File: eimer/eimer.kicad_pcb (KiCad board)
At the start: 2 copper layers, 21 x 51 mm, 33 parts, among them J1 Conn_01x20, J2 Conn_01x20, J3 Conn_01x03, J4 USB_C_Receptacle_USB2.0_14P, SW1 SW_Push, U1 RP2040, U2 MCP1700x-330xxTT, U4 W25Q16JVUXIQ TR, Y1 12 MHz

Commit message: more routing
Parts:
- moved R1 21.9 mm to (163.9, 72.9), turned to -90 degrees
- moved R2 19.8 mm to (160.8, 72.9), turned to 90 degrees
- moved C4 4.76 mm to (163.2, 83.8)
- moved C3 4.68 mm to (164.2, 83.1)
- moved C11 4.67 mm to (162.2, 83.5)
- moved C2 3.24 mm to (166.2, 87.3)
- moved C12 3.05 mm to (165.2, 86.9)
- moved R5 1.84 mm to (162.8, 97.0), turned to 180 degrees
- moved U2 1.61 mm to (159.5, 75.8)
- moved R7 1.59 mm to (158.0, 82.0)
- moved C17 1.32 mm to (160.3, 82.0), turned to 180 degrees
- moved C8 1.21 mm to (157.7, 88.5)
- moved C15 1.11 mm to (159.1, 99.4)
- moved C13 1.08 mm to (158.7, 72.7), turned to 180 degrees
- moved Y1 0.74 mm to (161.7, 99.4)
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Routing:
- net +3.3V: track 0.00 -> 22.8 mm, vias 0 -> 2
- net XIN: track 0.00 -> 6.99 mm
- net +1V1: track 0.00 -> 6.34 mm
- net Net-(C16-Pad1): track 0.00 -> 3.40 mm
- net GND: track 0.00 -> 3.36 mm
- net Net-(J4-CC1): track 0.00 -> 1.90 mm
- net Net-(J4-CC2): track 0.00 -> 1.83 mm
- net XOUT: track 0.00 -> 1.60 mm
- net Net-(U1-USB_DP): track 1.40 -> 0.00 mm
- net Net-(U1-USB_DM): track 1.40 -> 0.00 mm
- net QSPI_SS: track 7.60 -> 8.88 mm
- net USB_D+: track 18.6 -> 19.5 mm
- net USB_D-: track 18.9 -> 19.4 mm

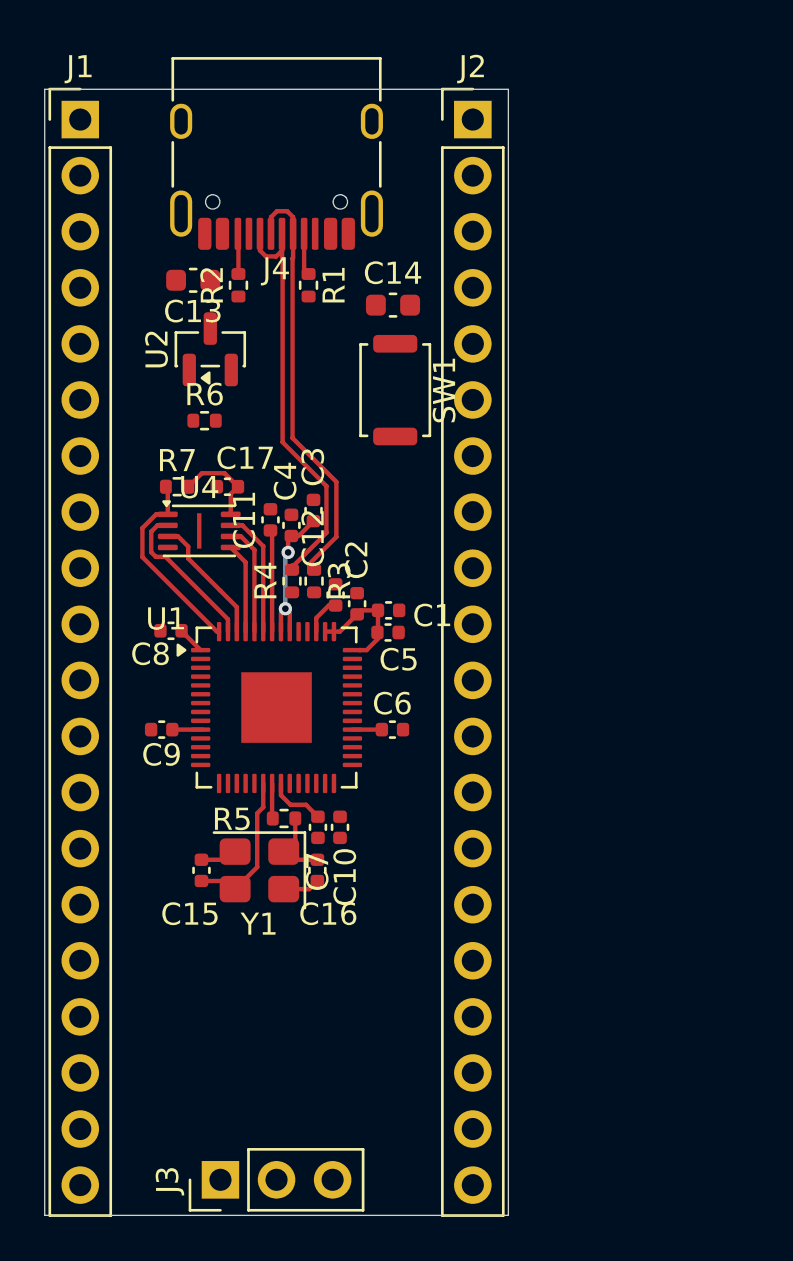
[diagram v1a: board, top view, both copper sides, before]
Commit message: routed left hand side gpios
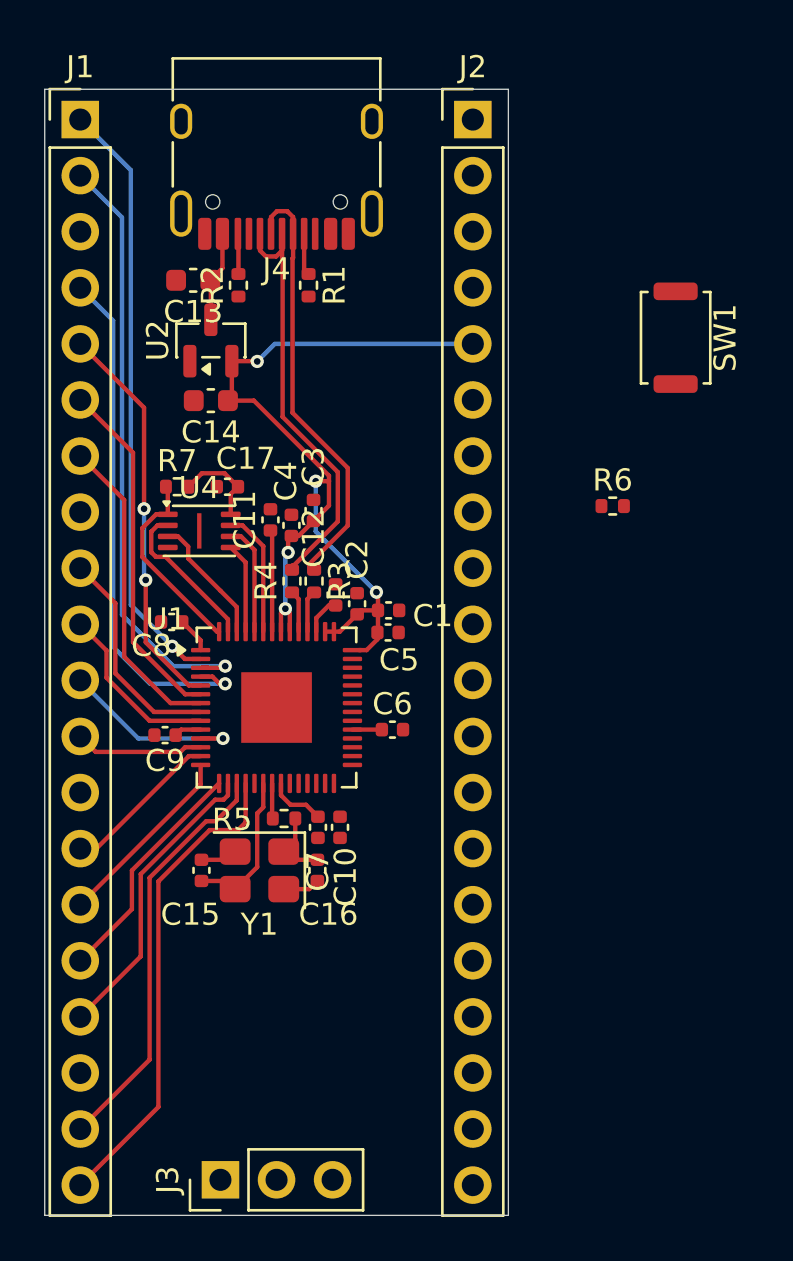
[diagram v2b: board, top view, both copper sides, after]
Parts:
- moved R6 18.9 mm to (177.7, 82.9)
- moved SW1 12.9 mm to (180.6, 75.2)
- moved C14 9.31 mm to (159.5, 78.1), turned to 180 degrees
- moved C8 0.40 mm to (157.8, 88.1)
- moved U2 0.40 mm to (159.5, 75.4)
- moved C9 0.29 mm to (157.4, 93.2)
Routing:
- net +3.3V: track 22.8 -> 52.1 mm, vias 2 -> 5
- net GPIO1: track 0.00 -> 27.5 mm, vias 0 -> 1
- net GPIO0: track 0.00 -> 27.1 mm, vias 0 -> 1
- net GPIO2: track 0.00 -> 23.9 mm, vias 0 -> 1
- net GPIO15: track 0.00 -> 22.0 mm
- net GPIO14: track 0.00 -> 18.8 mm
- net GPIO3: track 0.00 -> 18.0 mm, vias 0 -> 2
- net GPIO4: track 0.00 -> 16.0 mm
- net GPIO5: track 0.00 -> 14.2 mm
- net GPIO13: track 0.00 -> 13.6 mm
- net GPIO12: track 0.00 -> 10.6 mm
- net GPIO6: track 0.00 -> 10.0 mm
- net GPIO11: track 0.00 -> 8.59 mm
- net GPIO8: track 0.00 -> 8.57 mm, vias 0 -> 1
- net GPIO7: track 0.00 -> 7.98 mm
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
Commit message: routed left hand gpios
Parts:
- moved C6 0.61 mm to (168.3, 93.3)
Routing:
- net GPIO29/ADC3: track 0.00 -> 24.9 mm, vias 0 -> 1
- net SWCLK: track 0.00 -> 21.4 mm, vias 0 -> 1
- net GPIO16: track 0.00 -> 21.3 mm
- net GPIO28/ADC2: track 0.00 -> 20.7 mm, vias 0 -> 1
- net SWDIO: track 0.00 -> 20.4 mm, vias 0 -> 1
- net GPIO17: track 0.00 -> 18.8 mm
- net GPIO27/ADC1: track 0.00 -> 16.4 mm
- net VBUS: track 4.13 -> 19.8 mm
- net GPIO26/ADC0: track 0.00 -> 14.4 mm
- net GPIO18: track 0.00 -> 13.9 mm
- net GPIO19: track 0.00 -> 11.8 mm
- net GPIO24: track 0.00 -> 10.4 mm
- net GPIO20: track 0.00 -> 9.80 mm
- net RUN: track 0.00 -> 9.46 mm, vias 0 -> 1
- net GPIO23: track 0.00 -> 8.71 mm
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
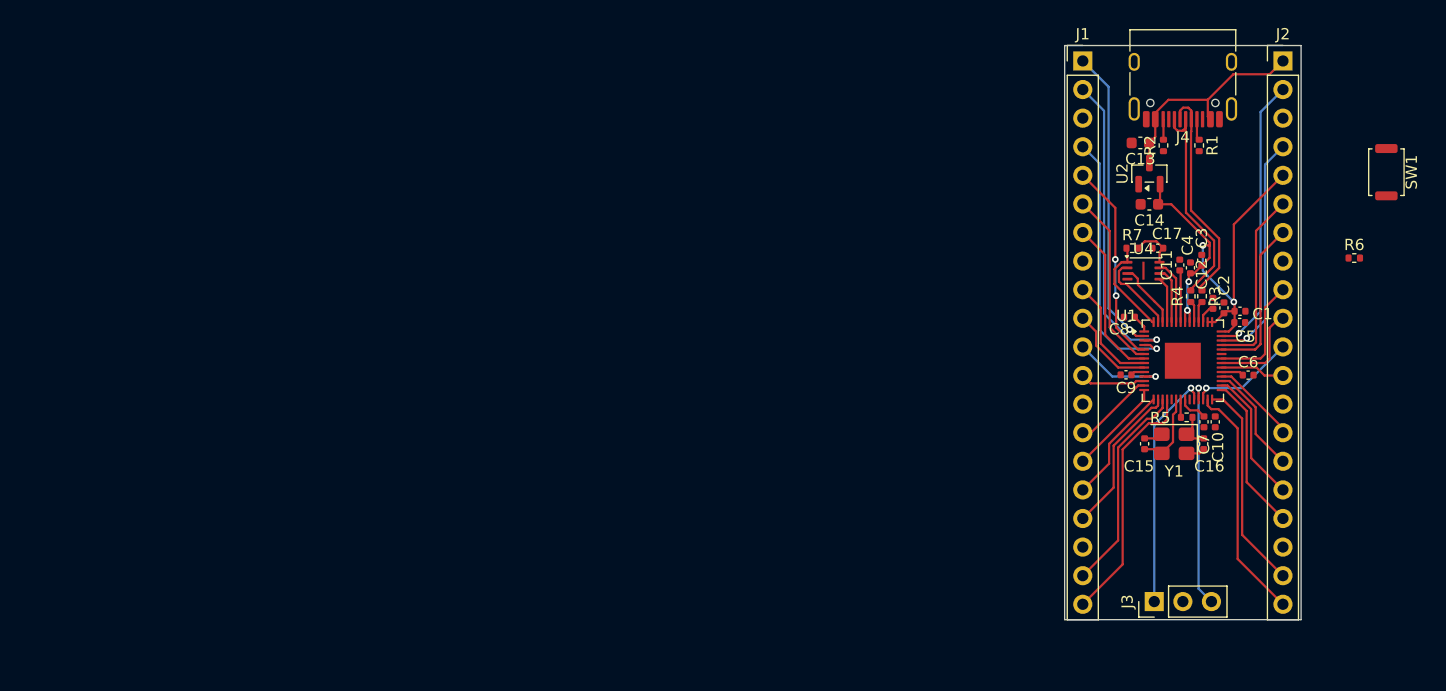
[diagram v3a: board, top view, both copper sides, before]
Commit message: finished schematic for wearable mcu
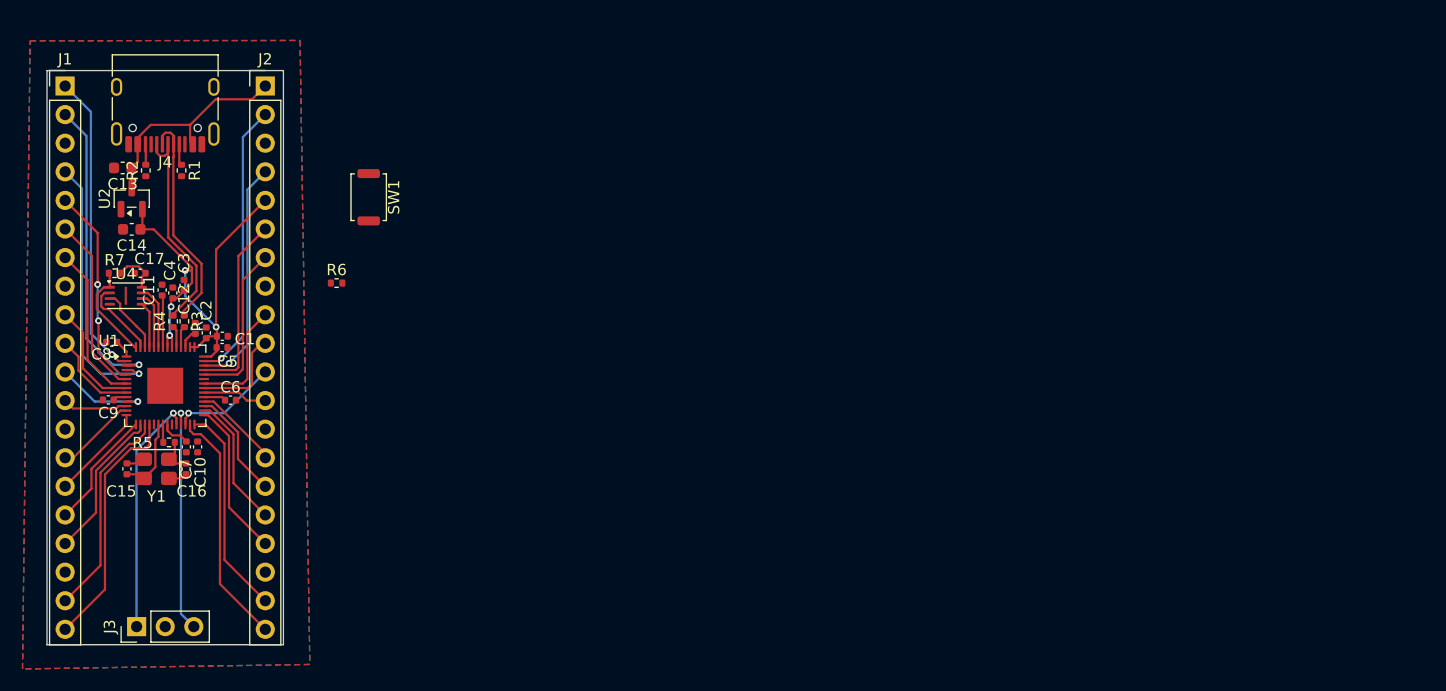
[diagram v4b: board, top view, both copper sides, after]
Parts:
- moved C12 90.4 mm to (74.8, 89.1)
- moved C3 90.4 mm to (73.8, 85.3)
- moved C4 90.4 mm to (72.8, 86.0)
- moved C5 90.4 mm to (77.2, 90.8)
- moved C6 90.4 mm to (77.9, 95.5)
- moved C10 90.4 mm to (75.0, 99.6)
- moved C14 90.4 mm to (69.1, 80.3)
- moved C17 90.4 mm to (69.9, 84.2)
- moved C2 90.4 mm to (75.8, 89.5)
- moved C7 90.4 mm to (74.0, 99.6)
- moved C8 90.4 mm to (67.4, 90.3)
- moved J1 90.4 mm to (63.2, 67.6)
- moved J3 90.4 mm to (69.6, 115.6)
- moved J4 90.4 mm to (72.1, 68.7)
- moved R2 90.4 mm to (70.4, 75.1)
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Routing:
- added copper zone on B.Cu, net GND
- added copper zone on F.Cu, net GND
